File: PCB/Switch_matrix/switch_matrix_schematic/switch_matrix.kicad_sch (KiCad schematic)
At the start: 18 parts

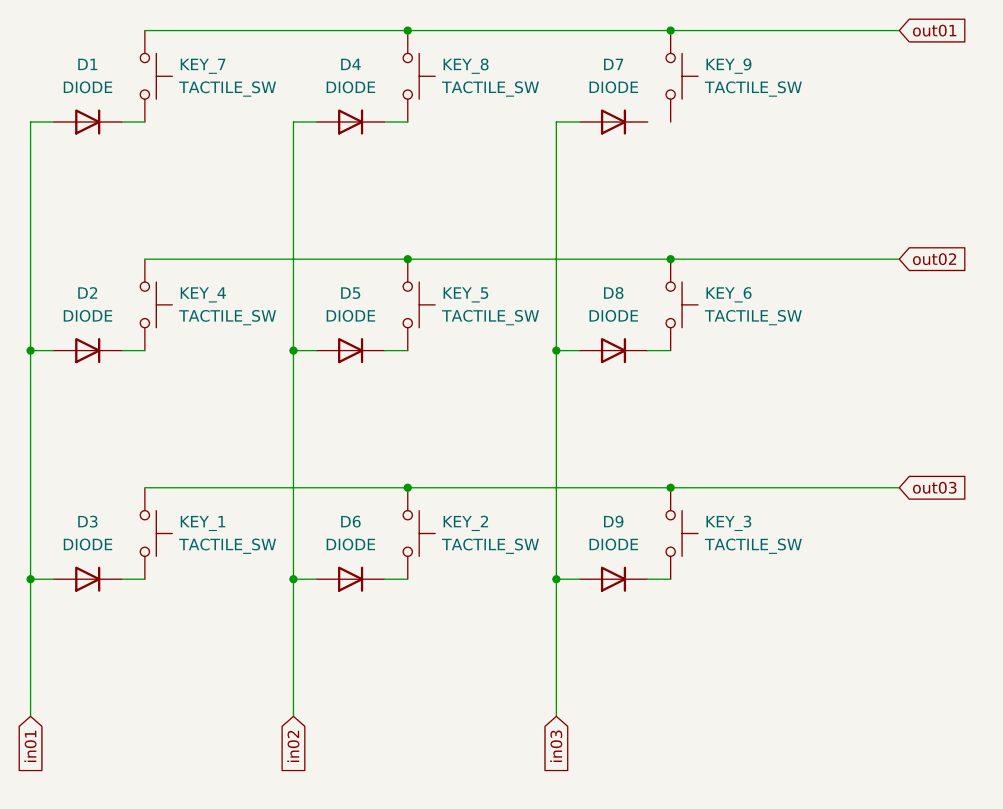
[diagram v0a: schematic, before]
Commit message: Renamed schematic components
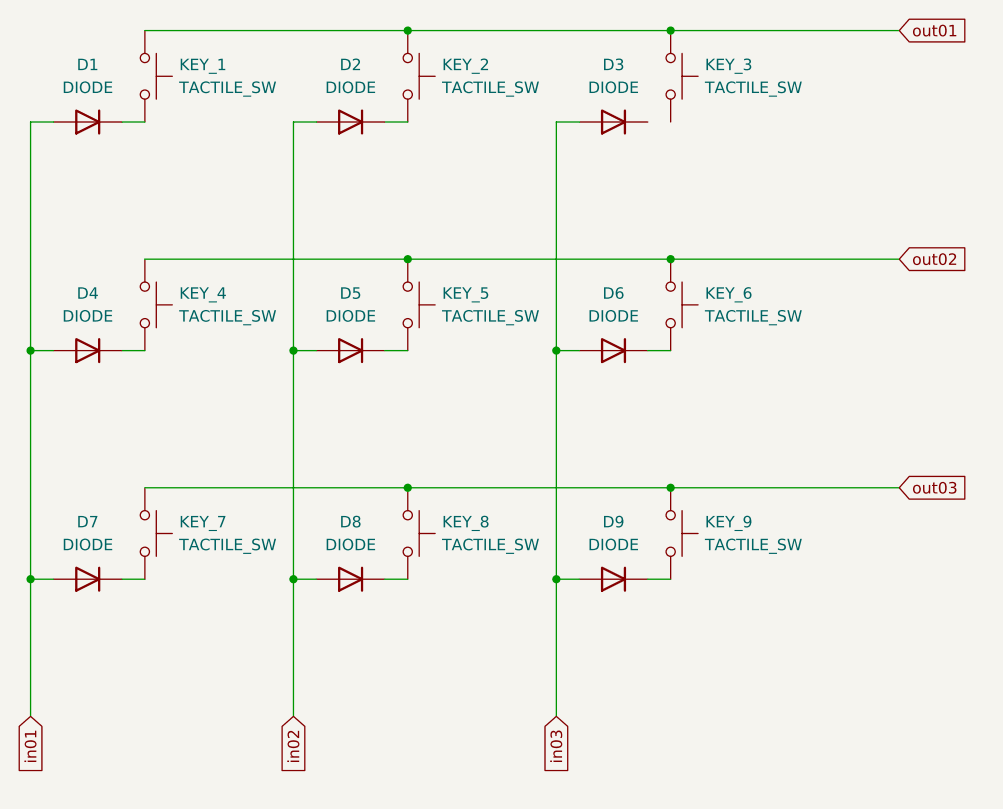
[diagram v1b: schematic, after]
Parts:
- renumbered D4 to D2, D7 to D3, D2 to D4, D8 to D6, D3 to D7, D6 to D8, KEY_7 to KEY_1, KEY_8 to KEY_2, KEY_9 to KEY_3, KEY_1 to KEY_7, KEY_2 to KEY_8, KEY_3 to KEY_9
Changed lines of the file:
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@@
   (symbol (lib_id "Simulation_SPICE:DIODE") (at 91.44 111.76 0) (unit 1)
     (in_bom yes) (on_board yes) (fields_autoplaced)
-    (property "Reference" "D3" (id 0) (at 91.44 105.41 0))
+    (property "Reference" "D7" (id 0) (at 91.44 105.41 0))
     (property "Value" "DIODE" (id 1) (at 91.44 107.95 0))
     (property "Footprint" "" (id 2) (at 91.44 111.76 0)
@@
   (symbol (lib_id "Switch:SW_MEC_5G") (at 156.21 55.88 270) (unit 1)
     (in_bom yes) (on_board yes) (fields_autoplaced)
-    (property "Reference" "KEY_9" (id 0) (at 160.02 54.6099 90)
+    (property "Reference" "KEY_3" (id 0) (at 160.02 54.6099 90)
       (effects (font (size 1.27 1.27)) (justify left))
     )
@@
   (symbol (lib_id "Simulation_SPICE:DIODE") (at 91.44 86.36 0) (unit 1)
     (in_bom yes) (on_board yes) (fields_autoplaced)
-    (property "Reference" "D2" (id 0) (at 91.44 80.01 0))
+    (property "Reference" "D4" (id 0) (at 91.44 80.01 0))
     (property "Value" "DIODE" (id 1) (at 91.44 82.55 0))
     (property "Footprint" "" (id 2) (at 91.44 86.36 0)
@@
   (symbol (lib_id "Simulation_SPICE:DIODE") (at 120.65 60.96 0) (unit 1)
     (in_bom yes) (on_board yes) (fields_autoplaced)
-    (property "Reference" "D4" (id 0) (at 120.65 54.61 0))
+    (property "Reference" "D2" (id 0) (at 120.65 54.61 0))
     (property "Value" "DIODE" (id 1) (at 120.65 57.15 0))
     (property "Footprint" "" (id 2) (at 120.65 60.96 0)
@@
   (symbol (lib_id "Switch:SW_MEC_5G") (at 156.21 106.68 270) (unit 1)
     (in_bom yes) (on_board yes) (fields_autoplaced)
-    (property "Reference" "KEY_3" (id 0) (at 160.02 105.4099 90)
+    (property "Reference" "KEY_9" (id 0) (at 160.02 105.4099 90)
       (effects (font (size 1.27 1.27)) (justify left))
     )
@@
   (symbol (lib_id "Switch:SW_MEC_5G") (at 127 106.68 270) (unit 1)
     (in_bom yes) (on_board yes) (fields_autoplaced)
-    (property "Reference" "KEY_2" (id 0) (at 130.81 105.4099 90)
+    (property "Reference" "KEY_8" (id 0) (at 130.81 105.4099 90)
       (effects (font (size 1.27 1.27)) (justify left))
     )
@@
   (symbol (lib_id "Simulation_SPICE:DIODE") (at 149.86 60.96 0) (unit 1)
     (in_bom yes) (on_board yes) (fields_autoplaced)
-    (property "Reference" "D7" (id 0) (at 149.86 54.61 0))
+    (property "Reference" "D3" (id 0) (at 149.86 54.61 0))
     (property "Value" "DIODE" (id 1) (at 149.86 57.15 0))
     (property "Footprint" "" (id 2) (at 149.86 60.96 0)
@@
   (symbol (lib_id "Simulation_SPICE:DIODE") (at 120.65 111.76 0) (unit 1)
     (in_bom yes) (on_board yes) (fields_autoplaced)
-    (property "Reference" "D6" (id 0) (at 120.65 105.41 0))
+    (property "Reference" "D8" (id 0) (at 120.65 105.41 0))
     (property "Value" "DIODE" (id 1) (at 120.65 107.95 0))
     (property "Footprint" "" (id 2) (at 120.65 111.76 0)
@@
   (symbol (lib_id "Switch:SW_MEC_5G") (at 97.79 55.88 270) (unit 1)
     (in_bom yes) (on_board yes) (fields_autoplaced)
-    (property "Reference" "KEY_7" (id 0) (at 101.6 54.6099 90)
+    (property "Reference" "KEY_1" (id 0) (at 101.6 54.6099 90)
       (effects (font (size 1.27 1.27)) (justify left))
     )
@@
   (symbol (lib_id "Switch:SW_MEC_5G") (at 127 55.88 270) (unit 1)
     (in_bom yes) (on_board yes) (fields_autoplaced)
-    (property "Reference" "KEY_8" (id 0) (at 130.81 54.6099 90)
+    (property "Reference" "KEY_2" (id 0) (at 130.81 54.6099 90)
       (effects (font (size 1.27 1.27)) (justify left))
     )
@@
   (symbol (lib_id "Switch:SW_MEC_5G") (at 97.79 106.68 270) (unit 1)
     (in_bom yes) (on_board yes) (fields_autoplaced)
-    (property "Reference" "KEY_1" (id 0) (at 101.6 105.4099 90)
+    (property "Reference" "KEY_7" (id 0) (at 101.6 105.4099 90)
       (effects (font (size 1.27 1.27)) (justify left))
     )
@@
   (symbol (lib_id "Simulation_SPICE:DIODE") (at 149.86 86.36 0) (unit 1)
     (in_bom yes) (on_board yes) (fields_autoplaced)
-    (property "Reference" "D8" (id 0) (at 149.86 80.01 0))
+    (property "Reference" "D6" (id 0) (at 149.86 80.01 0))
     (property "Value" "DIODE" (id 1) (at 149.86 82.55 0))
     (property "Footprint" "" (id 2) (at 149.86 86.36 0)
@@
       (reference "D1") (unit 1) (value "DIODE") (footprint "")
     )
+    (path "/2e3bce25-6423-49c6-99d7-7d704bdc7d75"
+      (reference "D2") (unit 1) (value "DIODE") (footprint "")
+    )
+    (path "/7e551f35-d67f-4e67-b9a8-31671023d5d8"
+      (reference "D3") (unit 1) (value "DIODE") (footprint "")
+    )
     (path "/1f3986d2-5d12-4a4d-b248-97f46b45b23b"
-      (reference "D2") (unit 1) (value "DIODE") (footprint "")
-    )
-    (path "/127c8326-2cd8-42b8-8a03-c8cdd6470af4"
-      (reference "D3") (unit 1) (value "DIODE") (footprint "")
-    )
-    (path "/2e3bce25-6423-49c6-99d7-7d704bdc7d75"
       (reference "D4") (unit 1) (value "DIODE") (footprint "")
     )
@@
       (reference "D5") (unit 1) (value "DIODE") (footprint "")
     )
+    (path "/f098c072-d93d-4393-afab-1e39f46fcd02"
+      (reference "D6") (unit 1) (value "DIODE") (footprint "")
+    )
+    (path "/127c8326-2cd8-42b8-8a03-c8cdd6470af4"
+      (reference "D7") (unit 1) (value "DIODE") (footprint "")
+    )
     (path "/980037b3-d941-41f1-82a1-e73ec8d6ca1f"
-      (reference "D6") (unit 1) (value "DIODE") (footprint "")
-    )
-    (path "/7e551f35-d67f-4e67-b9a8-31671023d5d8"
-      (reference "D7") (unit 1) (value "DIODE") (footprint "")
-    )
-    (path "/f098c072-d93d-4393-afab-1e39f46fcd02"
       (reference "D8") (unit 1) (value "DIODE") (footprint "")
     )
@@
       (reference "D9") (unit 1) (value "DIODE") (footprint "")
     )
-    (path "/e3c8d079-a354-4bfa-ab43-27892078d4a1"
+    (path "/994d28a0-2d62-48d4-b9ad-1ca28c8ec712"
       (reference "KEY_1") (unit 1) (value "TACTILE_SW") (footprint "")
     )
-    (path "/6c7f4ba4-579f-40e3-b5ee-2f8d3090d04d"
+    (path "/9e88ffa1-1f18-40c1-953c-1970d56a2608"
       (reference "KEY_2") (unit 1) (value "TACTILE_SW") (footprint "")
     )
-    (path "/409533fd-1675-4046-b5f9-44ec7e11ffeb"
+    (path "/130bb712-41cc-491e-827e-bb9a11451ade"
       (reference "KEY_3") (unit 1) (value "TACTILE_SW") (footprint "")
     )
@@
       (reference "KEY_6") (unit 1) (value "TACTILE_SW") (footprint "")
     )
-    (path "/994d28a0-2d62-48d4-b9ad-1ca28c8ec712"
+    (path "/e3c8d079-a354-4bfa-ab43-27892078d4a1"
       (reference "KEY_7") (unit 1) (value "TACTILE_SW") (footprint "")
     )
-    (path "/9e88ffa1-1f18-40c1-953c-1970d56a2608"
+    (path "/6c7f4ba4-579f-40e3-b5ee-2f8d3090d04d"
       (reference "KEY_8") (unit 1) (value "TACTILE_SW") (footprint "")
     )
-    (path "/130bb712-41cc-491e-827e-bb9a11451ade"
+    (path "/409533fd-1675-4046-b5f9-44ec7e11ffeb"
       (reference "KEY_9") (unit 1) (value "TACTILE_SW") (footprint "")
     )
